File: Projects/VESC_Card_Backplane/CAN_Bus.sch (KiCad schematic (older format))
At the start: 0 parts

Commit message: Updated subsheets and added CAN bus :)
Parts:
- added P4: CONN_01X04, symbol CONN_01X04
- added R6: 120, symbol R
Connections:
- new net +5V: P4.1 (P1)
- new net CANH: P4.2 (P2), R6.1
- new net CANL: P4.3 (P3), R6.2
- new net GNDD: P4.4 (P4)
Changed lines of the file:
@@
 $Descr A4 11693 8268
 encoding utf-8
-Sheet 1 5
+Sheet 5 6
 Title ""
 Date ""
@@
 Comment4 ""
 $EndDescr
+Wire Wire Line
+	4850 3550 5225 3550
+Wire Wire Line
+	5225 3650 4900 3650
+$Comp
+L R R6
+U 1 1 58788FC5
+P 4675 3600
+F 0 "R6" V 4755 3600 50  0000 C CNN
+F 1 "120" V 4675 3600 50  0000 C CNN
+F 2 "" V 4605 3600 50  0000 C CNN
+F 3 "" H 4675 3600 50  0000 C CNN
+	1    4675 3600
+	1    0    0    -1
+$EndComp
+Wire Wire Line
+	4850 3450 4850 3550
+Wire Wire Line
+	4450 3450 4675 3450
+Wire Wire Line
+	4675 3450 4850 3450
+Wire Wire Line
+	4900 3650 4900 3750
+Wire Wire Line
+	4900 3750 4675 3750
+Wire Wire Line
+	4675 3750 4450 3750
+Connection ~ 4675 3750
+Connection ~ 4675 3450
+Text HLabel 4450 3450 0    60   Input ~ 0
+CANH
+Text HLabel 4450 3750 0    60   Input ~ 0
+CANL
+$Comp
+L CONN_01X04 P4
+U 1 1 58789187
+P 5425 3600
+F 0 "P4" H 5425 3850 50  0000 C CNN
+F 1 "CONN_01X04" V 5525 3600 50  0000 C CNN
+F 2 "" H 5425 3600 50  0000 C CNN
+F 3 "" H 5425 3600 50  0000 C CNN
+	1    5425 3600
+	1    0    0    -1
+$EndComp
+Wire Wire Line
+	5225 3450 5075 3450
+Wire Wire Line
+	5075 3450 5075 3250
+Wire Wire Line
+	5075 3250 4450 3250
+Wire Wire Line
+	5225 3750 5100 3750
+Wire Wire Line
+	5100 3750 5100 3925
+Wire Wire Line
+	5100 3925 4450 3925
+$Comp
+L +5V #PWR8
+U 1 1 587891D5
+P 4450 3250
+F 0 "#PWR8" H 4450 3100 50  0001 C CNN
+F 1 "+5V" H 4450 3390 50  0000 C CNN
+F 2 "" H 4450 3250 50  0000 C CNN
+F 3 "" H 4450 3250 50  0000 C CNN
+	1    4450 3250
+	1    0    0    -1
+$EndComp
+$Comp
+L GNDD #PWR9
+U 1 1 587891FF
+P 4450 3925
+F 0 "#PWR9" H 4450 3675 50  0001 C CNN
+F 1 "GNDD" H 4450 3775 50  0000 C CNN
+F 2 "" H 4450 3925 50  0000 C CNN
+F 3 "" H 4450 3925 50  0000 C CNN
+	1    4450 3925
+	1    0    0    -1
+$EndComp
 $EndSCHEMATC

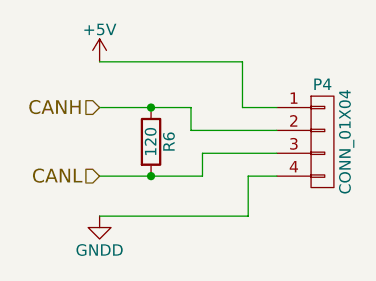
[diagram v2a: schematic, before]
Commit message: Footprint assoc. for backplane
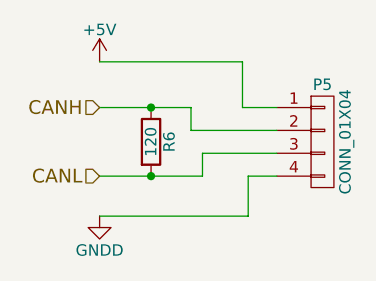
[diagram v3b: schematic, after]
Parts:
- P5: renamed from P4; footprint (none) -> USST-footprints:Molex_39502_1004R
- R6: footprint (none) -> Resistors_SMD:R_0805
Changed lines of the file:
@@
 F 0 "R6" V 4755 3600 50  0000 C CNN
 F 1 "120" V 4675 3600 50  0000 C CNN
-F 2 "" V 4605 3600 50  0000 C CNN
+F 2 "Resistors_SMD:R_0805" V 4605 3600 50  0001 C CNN
 F 3 "" H 4675 3600 50  0000 C CNN
 	1    4675 3600
@@
 	4850 3450 4850 3550
 Wire Wire Line
-	4450 3450 4675 3450
-Wire Wire Line
-	4675 3450 4850 3450
+	4450 3450 4850 3450
 Wire Wire Line
 	4900 3650 4900 3750
 Wire Wire Line
-	4900 3750 4675 3750
-Wire Wire Line
-	4675 3750 4450 3750
+	4900 3750 4450 3750
 Connection ~ 4675 3750
 Connection ~ 4675 3450
@@
 CANL
 $Comp
-L CONN_01X04 P4
+L CONN_01X04 P5
 U 1 1 58789187
 P 5425 3600
-F 0 "P4" H 5425 3850 50  0000 C CNN
+F 0 "P5" H 5425 3850 50  0000 C CNN
 F 1 "CONN_01X04" V 5525 3600 50  0000 C CNN
-F 2 "" H 5425 3600 50  0000 C CNN
+F 2 "USST-footprints:Molex_39502_1004R" H 5425 3600 50  0001 C CNN
 F 3 "" H 5425 3600 50  0000 C CNN
 	1    5425 3600
@@
 	5100 3925 4450 3925
 $Comp
-L +5V #PWR8
+L +5V #PWR014
 U 1 1 587891D5
 P 4450 3250
-F 0 "#PWR8" H 4450 3100 50  0001 C CNN
+F 0 "#PWR014" H 4450 3100 50  0001 C CNN
 F 1 "+5V" H 4450 3390 50  0000 C CNN
 F 2 "" H 4450 3250 50  0000 C CNN
@@
 $EndComp
 $Comp
-L GNDD #PWR9
+L GNDD #PWR015
 U 1 1 587891FF
 P 4450 3925
-F 0 "#PWR9" H 4450 3675 50  0001 C CNN
+F 0 "#PWR015" H 4450 3675 50  0001 C CNN
 F 1 "GNDD" H 4450 3775 50  0000 C CNN
 F 2 "" H 4450 3925 50  0000 C CNN

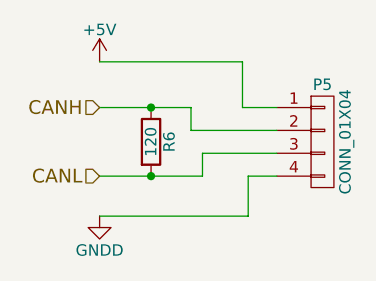
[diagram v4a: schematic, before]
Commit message: Finished connecting the components, just need to fix copper zones
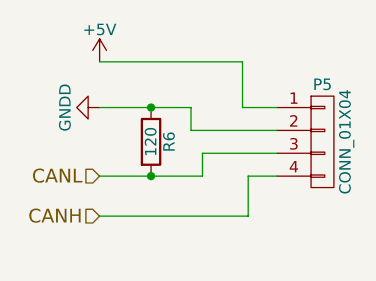
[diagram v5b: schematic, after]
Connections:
- net CANH: now also P5.4 (P4); no longer P5.2 (P2), R6.1
- net GNDD: now also P5.2 (P2), R6.1; no longer P5.4 (P4)
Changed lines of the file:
@@
 Connection ~ 4675 3750
 Connection ~ 4675 3450
-Text HLabel 4450 3450 0    60   Input ~ 0
+Text HLabel 4450 3925 0    60   Input ~ 0
 CANH
 Text HLabel 4450 3750 0    60   Input ~ 0
@@
 L GNDD #PWR012
 U 1 1 587891FF
-P 4450 3925
-F 0 "#PWR012" H 4450 3675 50  0001 C CNN
-F 1 "GNDD" H 4450 3775 50  0000 C CNN
-F 2 "" H 4450 3925 50  0000 C CNN
-F 3 "" H 4450 3925 50  0000 C CNN
-	1    4450 3925
-	1    0    0    -1
+P 4450 3450
+F 0 "#PWR012" H 4450 3200 50  0001 C CNN
+F 1 "GNDD" H 4450 3300 50  0000 C CNN
+F 2 "" H 4450 3450 50  0000 C CNN
+F 3 "" H 4450 3450 50  0000 C CNN
+	1    4450 3450
+	0    1    1    0
 $EndComp
 $EndSCHEMATC

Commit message: sync for working with liz
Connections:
- net CANH: now also R6.2
- net CANL: now also R6.1; no longer R6.2
- net GNDD: no longer R6.1
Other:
- moved on the sheet: R6
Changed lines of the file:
@@
 L R R6
 U 1 1 58788FC5
-P 4675 3600
-F 0 "R6" V 4755 3600 50  0000 C CNN
-F 1 "120" V 4675 3600 50  0000 C CNN
-F 2 "Resistors_SMD:R_0805" V 4605 3600 50  0001 C CNN
-F 3 "" H 4675 3600 50  0000 C CNN
-	1    4675 3600
+P 4675 3900
+F 0 "R6" H 4755 3900 50  0000 C CNN
+F 1 "120" V 4675 3900 50  0000 C CNN
+F 2 "Resistors_SMD:R_0805" V 4605 3900 50  0001 C CNN
+F 3 "" H 4675 3900 50  0000 C CNN
+	1    4675 3900
 	1    0    0    -1
 $EndComp
@@
 	4450 3450 4850 3450
 Wire Wire Line
-	4900 3650 4900 3750
+	4900 3750 4900 3650
 Wire Wire Line
-	4900 3750 4450 3750
+	4450 3750 4900 3750
 Connection ~ 4675 3750
-Connection ~ 4675 3450
-Text HLabel 4450 3925 0    60   Input ~ 0
+Text HLabel 4450 4050 0    60   Input ~ 0
 CANH
 Text HLabel 4450 3750 0    60   Input ~ 0
@@
 	5225 3750 5100 3750
 Wire Wire Line
-	5100 3750 5100 3925
+	5100 3750 5100 4050
 Wire Wire Line
-	5100 3925 4450 3925
+	5100 4050 4450 4050
 $Comp
 L +5V #PWR011
@@
 	0    1    1    0
 $EndComp
+Connection ~ 4675 4050
 $EndSCHEMATC

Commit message: Added copper zones in VESC Backplane
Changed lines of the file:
@@
 	4450 3450 4850 3450
 Wire Wire Line
-	4900 3750 4900 3650
+	4900 3650 4900 3750
 Wire Wire Line
-	4450 3750 4900 3750
+	4900 3750 4450 3750
 Connection ~ 4675 3750
 Text HLabel 4450 4050 0    60   Input ~ 0
